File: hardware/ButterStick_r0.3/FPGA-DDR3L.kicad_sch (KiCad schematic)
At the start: 8 parts, among them U4 ECP5UM5G_85_CABGA381, X1 ASDMB

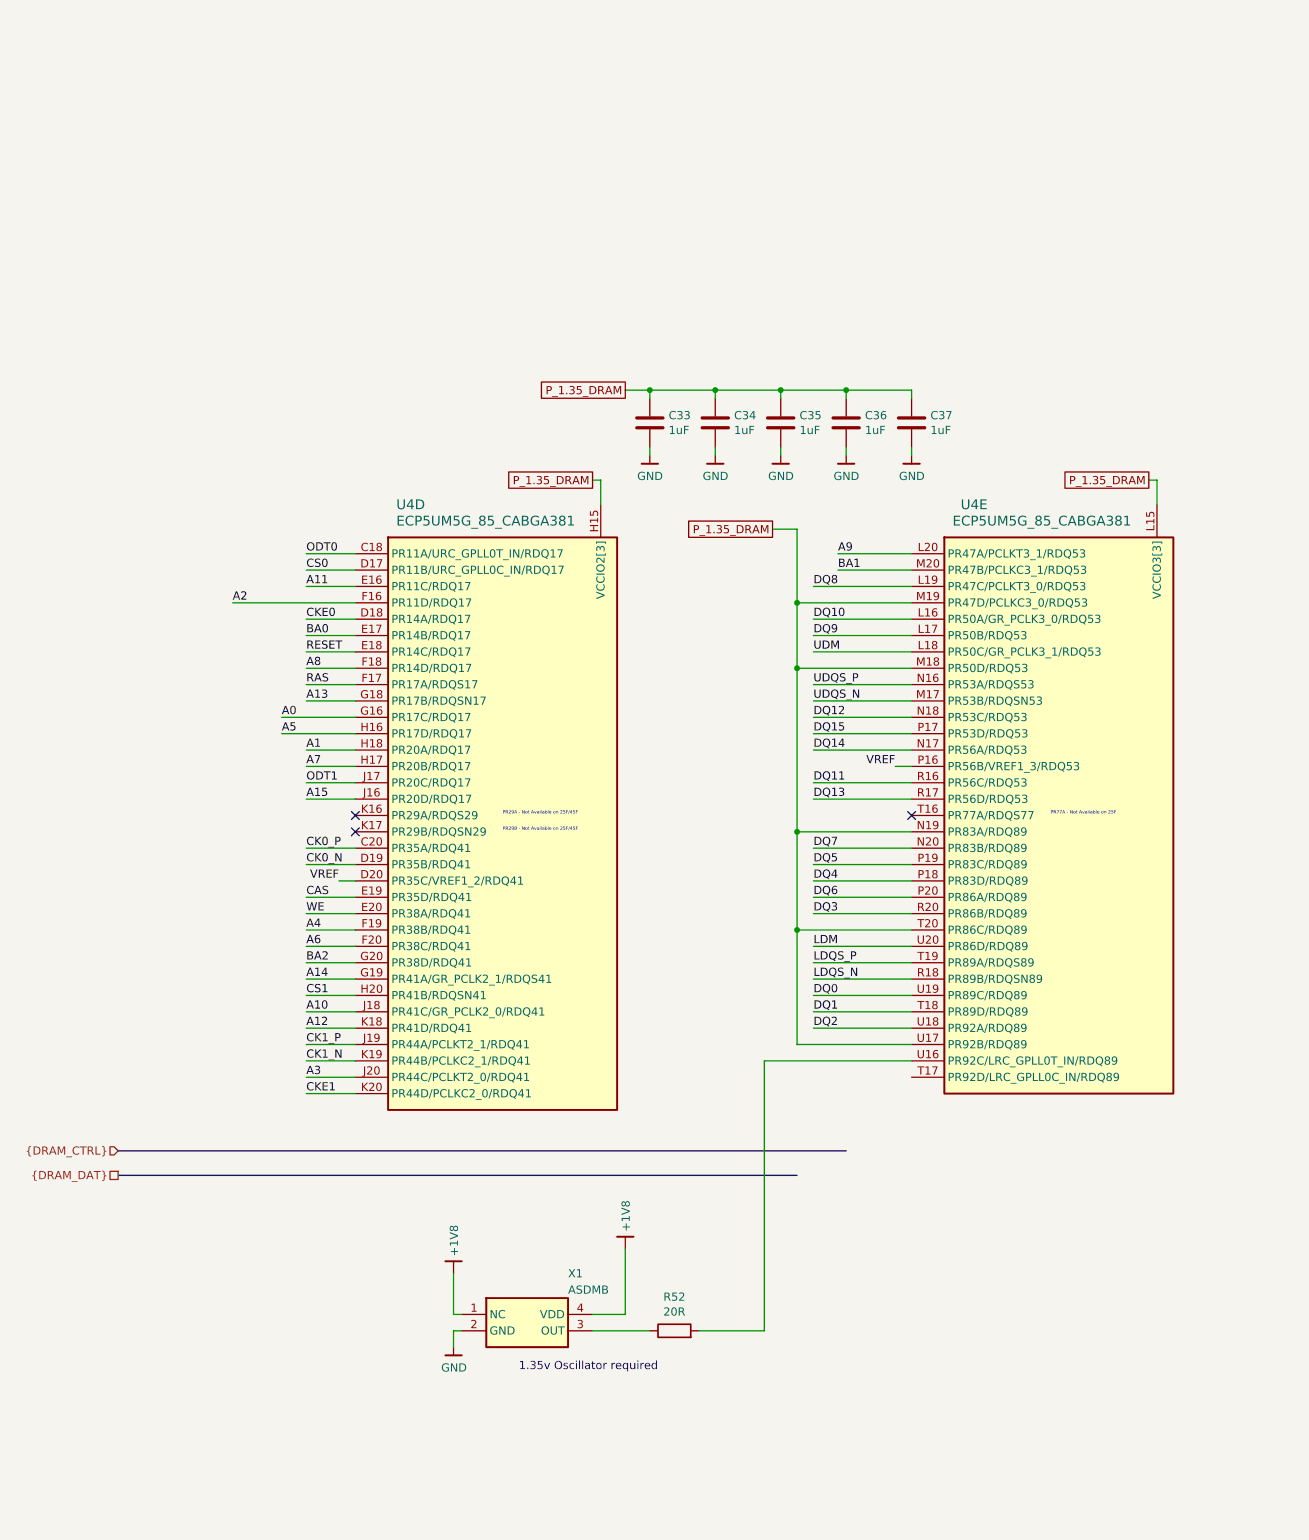
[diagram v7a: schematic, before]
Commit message: hw.r0d3: Continue routing
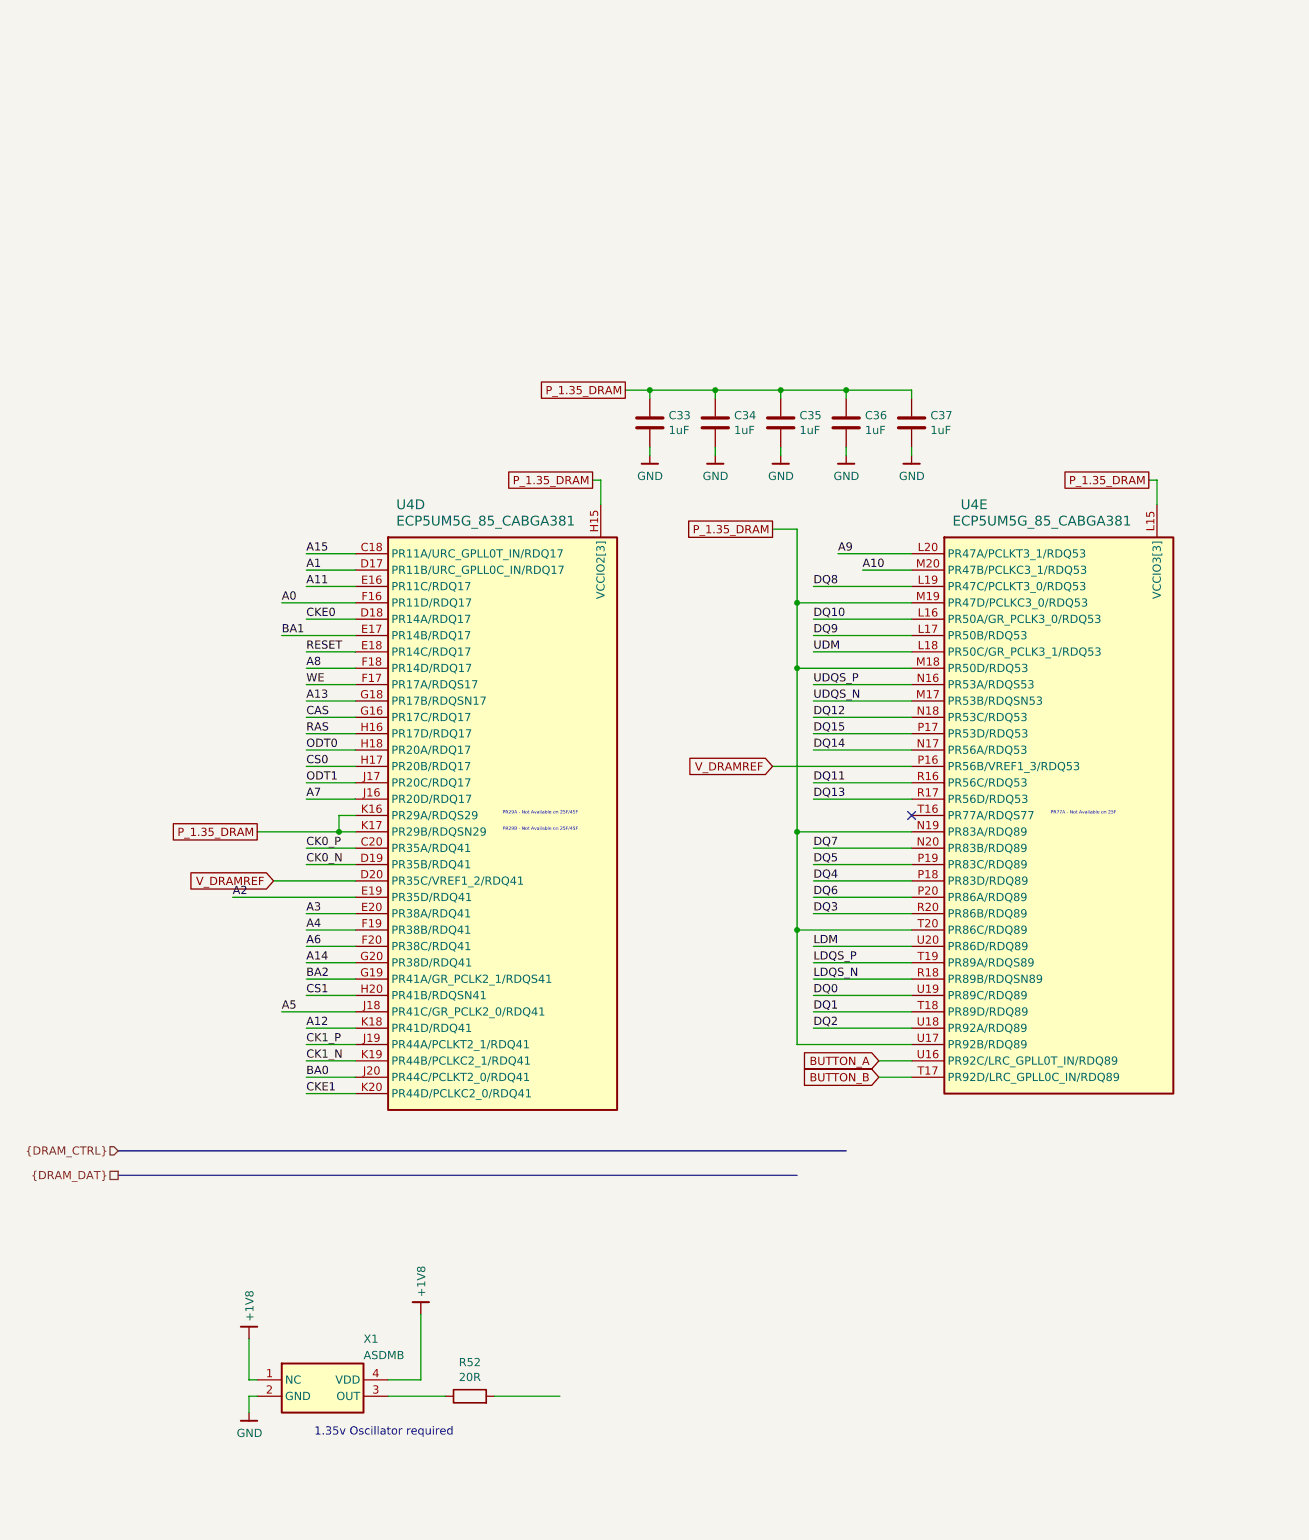
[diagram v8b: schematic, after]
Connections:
- net A0: now also U4.F16 (PR11D/RDQ17); no longer U4.G16 (PR17C/RDQ17)
- net A1: now also U4.D17 (PR11B/URC_GPLL0C_IN/RDQ17); no longer U4.H18 (PR20A/RDQ17)
- net A10: now also U4.M20 (PR47B/PCLKC3_1/RDQ53); no longer U4.J18 (PR41C/GR_PCLK2_0/RDQ41)
- net A14: now also U4.G20 (PR38D/RDQ41); no longer U4.G19 (PR41A/GR_PCLK2_1/RDQS41)
- net A15: now also U4.C18 (PR11A/URC_GPLL0T_IN/RDQ17); no longer U4.J16 (PR20D/RDQ17)
- net A2: now also U4.E19 (PR35D/RDQ41); no longer U4.F16 (PR11D/RDQ17)
- net A3: now also U4.E20 (PR38A/RDQ41); no longer U4.J20 (PR44C/PCLKT2_0/RDQ41)
- net A5: now also U4.J18 (PR41C/GR_PCLK2_0/RDQ41); no longer U4.H16 (PR17D/RDQ17)
- net A7: now also U4.J16 (PR20D/RDQ17); no longer U4.H17 (PR20B/RDQ17)
- net BA0: now also U4.J20 (PR44C/PCLKT2_0/RDQ41); no longer U4.E17 (PR14B/RDQ17)
- net BA1: now also U4.E17 (PR14B/RDQ17); no longer U4.M20 (PR47B/PCLKC3_1/RDQ53)
- net BA2: now also U4.G19 (PR41A/GR_PCLK2_1/RDQS41); no longer U4.G20 (PR38D/RDQ41)
- net CAS: now also U4.G16 (PR17C/RDQ17); no longer U4.E19 (PR35D/RDQ41)
- net CS0: now also U4.H17 (PR20B/RDQ17); no longer U4.D17 (PR11B/URC_GPLL0C_IN/RDQ17)
- net ODT0: now also U4.H18 (PR20A/RDQ17); no longer U4.C18 (PR11A/URC_GPLL0T_IN/RDQ17)
- net P_1.35_DRAM: now also U4.K16 (PR29A/RDQS29), U4.K17 (PR29B/RDQSN29)
- net RAS: now also U4.H16 (PR17D/RDQ17); no longer U4.F17 (PR17A/RDQS17)
- net WE: now also U4.F17 (PR17A/RDQS17); no longer U4.E20 (PR38A/RDQ41)
- net BUTTON_B: now reaches U4.T17 (PR92D/LRC_GPLL0C_IN/RDQ89)
- net at R52.2: no longer U4.U16 (PR92C/LRC_GPLL0T_IN/RDQ89)
- net VREF renamed V_DRAMREF
- new net BUTTON_A: U4.U16 (PR92C/LRC_GPLL0T_IN/RDQ89)
- no-connect marks 3 -> 1
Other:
- moved on the sheet: R52, X1
